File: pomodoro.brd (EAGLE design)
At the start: 105.1 x 61 mm, 26 parts, among them J1 POWER_JACK, J2 AVR_SPI_PROG_3X2PTH, U2 328P, Y1 16MHz

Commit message: Move parts a bit
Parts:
- R1, R2, R3, R4, R5, R6, R7, R8: value 10k -> 1k; device SparkFun-Resistors:AXIAL-0.3-KIT -> SparkFun-Resistors:AXIAL-0.3
- moved R7 43.2 mm to (33.0, 34.3)
- moved R8 43.2 mm to (25.4, 34.3)
- moved R2 20.3 mm to (76.2, 34.3)
- moved R3 20.3 mm to (68.6, 34.3)
- moved R4 15.2 mm to (55.9, 34.3)
- moved R6 15.2 mm to (40.6, 34.3)
- moved R5 15.2 mm to (48.3, 34.3)
- moved LS1 5.24 mm to (81.3, 57.1)
- moved C4 3.81 mm to (61.0, 54.6)
- moved C3 2.54 mm to (66.0, 54.6)
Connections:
- removed net N$20: S1.1, U2.23
- new net N$1: R2.P$2, RED_LED.K
- net N$10: now also S1.1, U2.15; no longer GREEN_LED.K, R8.P$2
- net N$4: now also GREEN_LED.K, R3.P$2; no longer D1.K, R2.P$2
- net N$5: now also D1.K, R4.P$2; no longer D2.K, R3.P$2
- net N$6: now also D2.K, R5.P$2; no longer D3.K, R4.P$2
- net N$7: now also D3.K, R6.P$2; no longer R7.P$2, RED_LED.K
- net N$8: now also R7.P$2; no longer R5.P$2
- net N$9: now also R8.P$2; no longer R6.P$2
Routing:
- net N$20: track 51.7 -> 0.00 mm
- net N$10: track 3.81 -> 39.8 mm
- net VCC: track 89.0 -> 95.1 mm
- net GND: track 215.9 -> 211.6 mm
- net N$1: track 0.00 -> 4.00 mm
- net N$18: track 16.3 -> 14.0 mm
- net N$3: track 13.6 -> 12.0 mm
- net RST: track 23.1 -> 24.6 mm
- net MISO: track 47.7 -> 49.1 mm
- net N$2: track 13.1 -> 12.0 mm

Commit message: Change layout
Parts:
- moved R2 68.7 mm to (19.1, 72.4), turned to 270 degrees
- moved R8 63.5 mm to (76.2, 72.4), turned to 270 degrees
- moved RED_LED 59.9 mm to (19.1, 61.0), turned to 90 degrees
- moved R3 55.7 mm to (27.9, 72.4), turned to 270 degrees
- moved D5 53.8 mm to (76.2, 61.0), turned to 90 degrees
- moved J2 51.5 mm to (7.62, 26.7), turned to 90 degrees
- moved R7 51.3 mm to (67.3, 72.4), turned to 270 degrees
- moved U2 44.9 mm to (39.4, 30.5), turned to 180 degrees
- moved GREEN_LED 44.4 mm to (27.9, 61.0), turned to 90 degrees
- moved R6 42.0 mm to (58.4, 72.4), turned to 270 degrees
- moved R4 41.0 mm to (40.6, 72.4), turned to 270 degrees
- moved D4 38.6 mm to (67.3, 61.0), turned to 90 degrees
- moved R5 38.1 mm to (49.5, 72.4), turned to 270 degrees
- moved Y1 35.9 mm to (33.0, 43.2), turned to 0 degrees
- moved C3 35.9 mm to (30.5, 49.5), turned to 270 degrees
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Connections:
- net N$18: now also U2.16; no longer U2.13
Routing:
- net N$18: track 14.0 -> 89.2 mm
- net N$10: track 39.8 -> 81.4 mm
- net RST: track 24.6 -> 53.6 mm
- net MISO: track 49.1 -> 25.0 mm
- net GND: track 211.6 -> 234.4 mm
- net SCK: track 47.3 -> 28.6 mm
- net MOSI: track 47.3 -> 34.7 mm
- net VCC: track 95.1 -> 107.3 mm
- net N$11: track 30.8 -> 36.4 mm
- net N$16: track 23.4 -> 27.5 mm
- net N$17: track 25.5 -> 29.1 mm
- net N$12: track 28.7 -> 32.2 mm
- net N$2: track 12.0 -> 15.2 mm
- net N$15: track 23.4 -> 26.5 mm
- net N$13: track 26.5 -> 29.6 mm
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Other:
- board text added: "5v"
- board text added: "gnd"

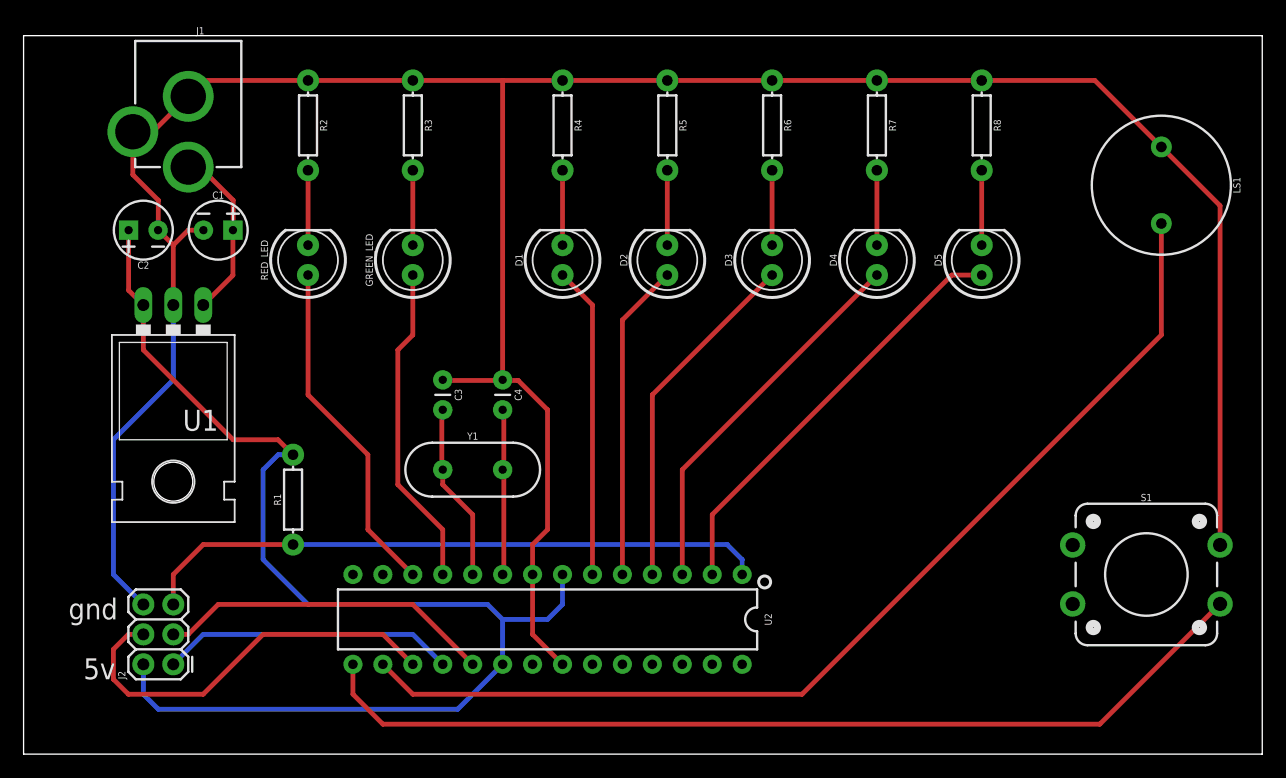
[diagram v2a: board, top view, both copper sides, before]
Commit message: Change values of elements
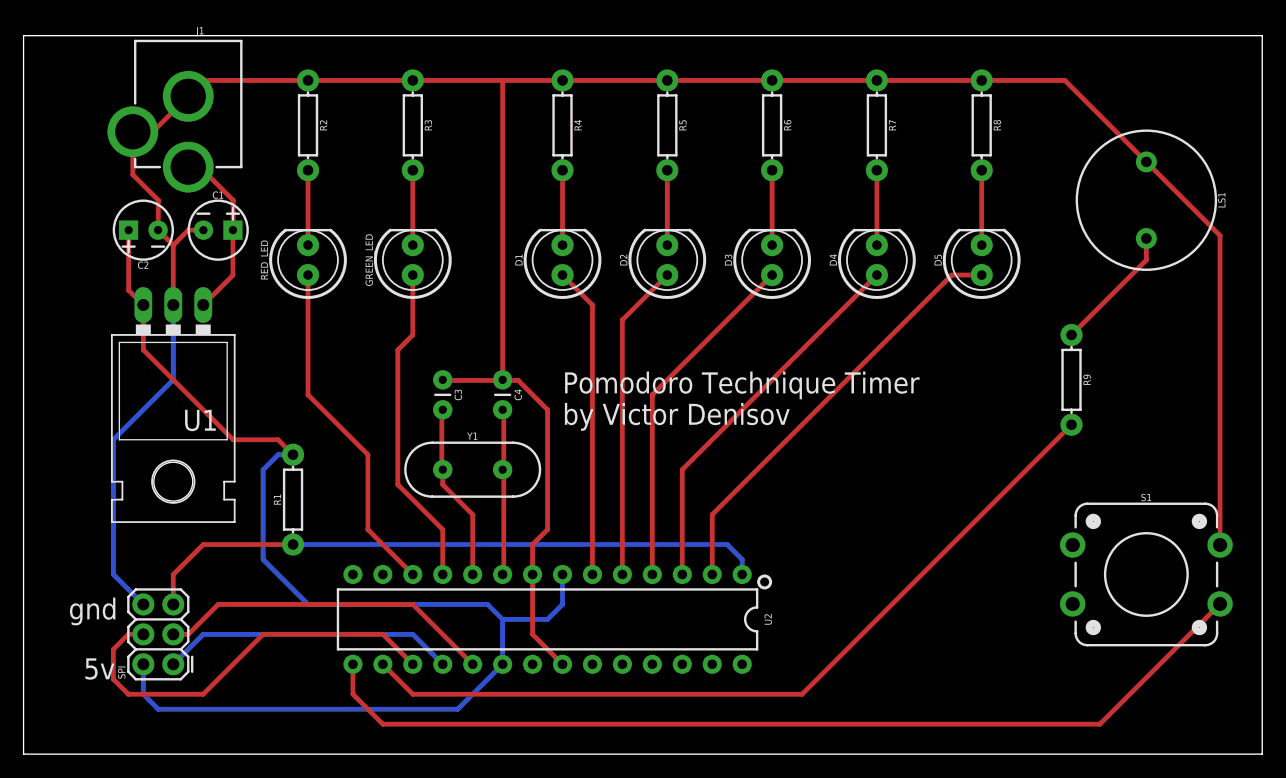
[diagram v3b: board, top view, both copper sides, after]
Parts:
- added R9: 100, SparkFun-Resistors:AXIAL-0.3
- C2: value 10uF -> 1uF
- R1: value 1k -> 10k
- moved LS1 1.80 mm to (90.2, 66.0)
- renumbered J2 to SPI
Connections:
- new net N$20: LS1.+, R9.P$1
- net N$18: now also R9.P$2; no longer LS1.+
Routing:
- net N$18: track 89.2 -> 68.9 mm
- net N$20: track 0.00 -> 10.8 mm
- net GND: track 234.4 -> 232.9 mm
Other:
- board text added: "Pomodoro Technique Timer by Victor Denisov"
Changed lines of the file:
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@@
 <text x="0" y="25.4" size="1.778" layer="21">5v</text>
 <text x="-1.27" y="30.48" size="1.778" layer="21">gnd</text>
+<text x="40.64" y="46.99" size="1.778" layer="21">Pomodoro Technique Timer
+by Victor Denisov</text>
 </plain>
 <attributes>
@@
 <attribute name="PROD_ID" value="CAP-08440" x="11.43" y="63.5" size="1.778" layer="27" display="off"/>
 </element>
-<element name="C2" library="SparkFun-Capacitors" package="CPOL-RADIAL-2.5MM-5MM" value="10uF" x="5.08" y="63.5" rot="R180">
+<element name="C2" library="SparkFun-Capacitors" package="CPOL-RADIAL-2.5MM-5MM" value="1uF" x="5.08" y="63.5" rot="R180">
 <attribute name="PROD_ID" value="CAP-08440" x="5.08" y="63.5" size="1.778" layer="27" rot="R180" display="off"/>
 </element>
@@
 <attribute name="PROD_ID" value="CONN-08197" x="8.89" y="82.55" size="1.778" layer="27" rot="R180" display="off"/>
 </element>
-<element name="J2" library="SparkFun-Connectors" package="2X3" value="AVR_SPI_PROG_3X2PTH" x="7.62" y="26.67" rot="R90"/>
-<element name="LS1" library="SparkFun-Electromechanical" package="BUZZER-12MM" value="BUZZER-PTH" x="91.44" y="67.31" rot="R270">
-<attribute name="PROD_ID" value="COMP-08253" x="91.44" y="67.31" size="1.778" layer="27" rot="R270" display="off"/>
-<attribute name="SF_SKU" value="COM-07950" x="91.44" y="67.31" size="1.778" layer="27" rot="R270" display="off"/>
+<element name="SPI" library="SparkFun-Connectors" package="2X3" value="AVR_SPI_PROG_3X2PTH" x="7.62" y="26.67" rot="R90"/>
+<element name="LS1" library="SparkFun-Electromechanical" package="BUZZER-12MM" value="BUZZER-PTH" x="90.17" y="66.04" rot="R270">
+<attribute name="PROD_ID" value="COMP-08253" x="90.17" y="66.04" size="1.778" layer="27" rot="R270" display="off"/>
+<attribute name="SF_SKU" value="COM-07950" x="90.17" y="66.04" size="1.778" layer="27" rot="R270" display="off"/>
 </element>
 <element name="RED_LED" library="SparkFun-LED" package="LED_5MM" value="" x="19.05" y="60.96" rot="R90"/>
@@
 <attribute name="PROD_ID" value="RES-12182" x="76.2" y="72.39" size="1.778" layer="27" rot="R270" display="off"/>
 </element>
-<element name="R1" library="SparkFun-Resistors" package="AXIAL-0.3" value="1k" x="17.78" y="40.64" rot="R90">
+<element name="R1" library="SparkFun-Resistors" package="AXIAL-0.3" value="10k" x="17.78" y="40.64" rot="R90">
 <attribute name="PROD_ID" value="RES-12182" x="17.78" y="40.64" size="1.778" layer="27" rot="R90" display="off"/>
+</element>
+<element name="R9" library="SparkFun-Resistors" package="AXIAL-0.3" value="100" x="83.82" y="50.8" rot="R270">
+<attribute name="PROD_ID" value="RES-12182" x="83.82" y="50.8" size="1.778" layer="27" rot="R270" display="off"/>
 </element>
 </elements>
@@
 <contactref element="C3" pad="1"/>
 <contactref element="C4" pad="1"/>
-<contactref element="LS1" pad="-"/>
 <contactref element="J1" pad="GNDBREAK"/>
 <contactref element="J1" pad="GND"/>
 <contactref element="U1" pad="GND"/>
 <contactref element="S1" pad="3"/>
-<contactref element="J2" pad="6"/>
+<contactref element="SPI" pad="6"/>
 <contactref element="R2" pad="P$1"/>
 <contactref element="R3" pad="P$1"/>
@@
 <wire x1="58.42" y1="76.2" x2="67.31" y2="76.2" width="0.4064" layer="1"/>
 <wire x1="67.31" y1="76.2" x2="76.2" y2="76.2" width="0.4064" layer="1"/>
-<wire x1="76.2" y1="76.2" x2="85.8" y2="76.2" width="0.4064" layer="1"/>
-<wire x1="85.8" y1="76.2" x2="91.44" y2="70.56" width="0.4064" layer="1"/>
-<wire x1="91.44" y1="70.56" x2="96.42" y2="65.58" width="0.4064" layer="1"/>
-<wire x1="96.42" y1="65.58" x2="96.42" y2="36.79" width="0.4064" layer="1"/>
+<contactref element="LS1" pad="-"/>
+<wire x1="76.2" y1="76.2" x2="83.26" y2="76.2" width="0.4064" layer="1"/>
+<wire x1="83.26" y1="76.2" x2="90.17" y2="69.29" width="0.4064" layer="1"/>
+<wire x1="90.17" y1="69.29" x2="96.42" y2="63.04" width="0.4064" layer="1"/>
+<wire x1="96.42" y1="63.04" x2="96.42" y2="36.79" width="0.4064" layer="1"/>
 </signal>
 <signal name="VCC">
@@
 <contactref element="C2" pad="1"/>
 <contactref element="U1" pad="OUT"/>
-<contactref element="J2" pad="2"/>
+<contactref element="SPI" pad="2"/>
 <contactref element="R1" pad="P$2"/>
 <wire x1="5.08" y1="26.67" x2="5.08" y2="24.13" width="0.4064" layer="16"/>
@@
 </signal>
 <signal name="MOSI">
-<contactref element="J2" pad="4"/>
+<contactref element="SPI" pad="4"/>
 <contactref element="U2" pad="17"/>
 <wire x1="5.08" y1="29.21" x2="3.81" y2="29.21" width="0.4064" layer="1"/>
@@
 </signal>
 <signal name="RST">
-<contactref element="J2" pad="5"/>
+<contactref element="SPI" pad="5"/>
 <contactref element="U2" pad="1"/>
 <contactref element="R1" pad="P$1"/>
@@
 </signal>
 <signal name="SCK">
-<contactref element="J2" pad="3"/>
+<contactref element="SPI" pad="3"/>
 <contactref element="U2" pad="19"/>
 <wire x1="7.62" y1="29.21" x2="8.89" y2="29.21" width="0.4064" layer="1"/>
@@
 </signal>
 <signal name="MISO">
-<contactref element="J2" pad="1"/>
+<contactref element="SPI" pad="1"/>
 <contactref element="U2" pad="18"/>
 <wire x1="7.62" y1="26.67" x2="10.16" y2="29.21" width="0.4064" layer="16"/>
@@
 <signal name="N$18">
 <contactref element="U2" pad="16"/>
-<contactref element="LS1" pad="+"/>
-<wire x1="91.44" y1="64.06" x2="91.44" y2="54.61" width="0.4064" layer="1"/>
-<wire x1="91.44" y1="54.61" x2="60.96" y2="24.13" width="0.4064" layer="1"/>
+<contactref element="R9" pad="P$2"/>
+<wire x1="83.82" y1="46.99" x2="60.96" y2="24.13" width="0.4064" layer="1"/>
 <wire x1="60.96" y1="24.13" x2="27.94" y2="24.13" width="0.4064" layer="1"/>
 <wire x1="27.94" y1="24.13" x2="25.4" y2="26.67" width="0.4064" layer="1"/>
+</signal>
+<signal name="N$20">
+<contactref element="R9" pad="P$1"/>
+<contactref element="LS1" pad="+"/>
+<wire x1="90.17" y1="62.79" x2="90.17" y2="60.96" width="0.4064" layer="1"/>
+<wire x1="90.17" y1="60.96" x2="83.82" y2="54.61" width="0.4064" layer="1"/>
 </signal>
 </signals>
 </board>
 </drawing>
+<compatibility>
+<note version="6.3" minversion="6.2.2" severity="warning">
+Since Version 6.2.2 text objects can contain more than one line,
+which will not be processed correctly with this version.
+</note>
+</compatibility>
 </eagle>
